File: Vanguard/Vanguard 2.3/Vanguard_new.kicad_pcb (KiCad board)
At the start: 4 copper layers, 42.1 x 52.7 mm, 85 parts, among them J1 USB_C_Receptacle_USB2.0_16P, J2 Conn_02x03_Pin, J3 Micro_SD_Card_Det1, J4 STARBOARD_SERVO, J5 PORTSIDE_SERVO, J6 Conn_01x02_Pin, J7 EJECTION_SERVO, Q1 BSS138, Q2 BSS138, Q3 BSS138, Q4 BSS138, U1 ATSAMD11D14A-M, U2 ATmega4809-A, U3 AT25DF641A-SH-T, U4 AP2112K-3.3, U5 BD1020HFV, U6 BNO086, U7 TXB0104D, U8 TPS61092, U9 MPM3610AGQV-P, Y1 32.768kHz

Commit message: done pcb
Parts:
- moved TP1 0.08 mm to (113.2, 92.5)
- moved TP2 0.05 mm to (114.7, 93.9)
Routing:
- net RX0: track 1.67 -> 41.4 mm, vias 0 -> 2
- net +3.3V: track 141.4 -> 167.0 mm, vias 14 -> 18
- net TX0: track 1.76 -> 23.2 mm, vias 0 -> 2
- net GND: track 104.7 -> 94.6 mm, vias 37 -> 41
- net Net-(D6-K): track 12.3 -> 15.6 mm
- net PORT_RED: track 27.0 -> 28.7 mm
- net CD: track 39.5 -> 40.7 mm
- net POWER_STAB: track 85.8 -> 86.9 mm
- net Net-(U9-EN): track 4.08 -> 4.92 mm
- net HOLD: track 16.1 -> 16.8 mm
- net PORT_SERVO: track 38.9 -> 39.5 mm
- removed copper zone on B.Cu, net (none)
- removed copper zone on F.Cu, net (none)

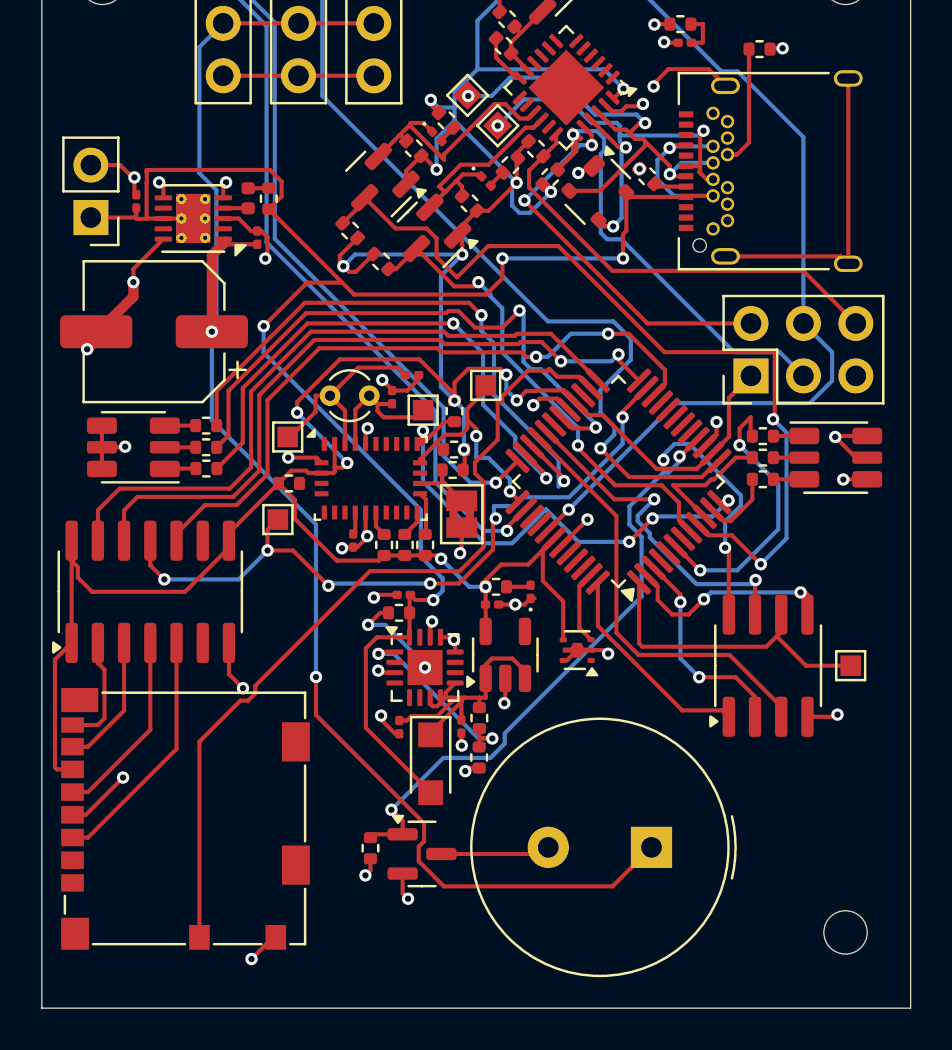
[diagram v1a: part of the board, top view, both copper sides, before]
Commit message: Centerd IMU
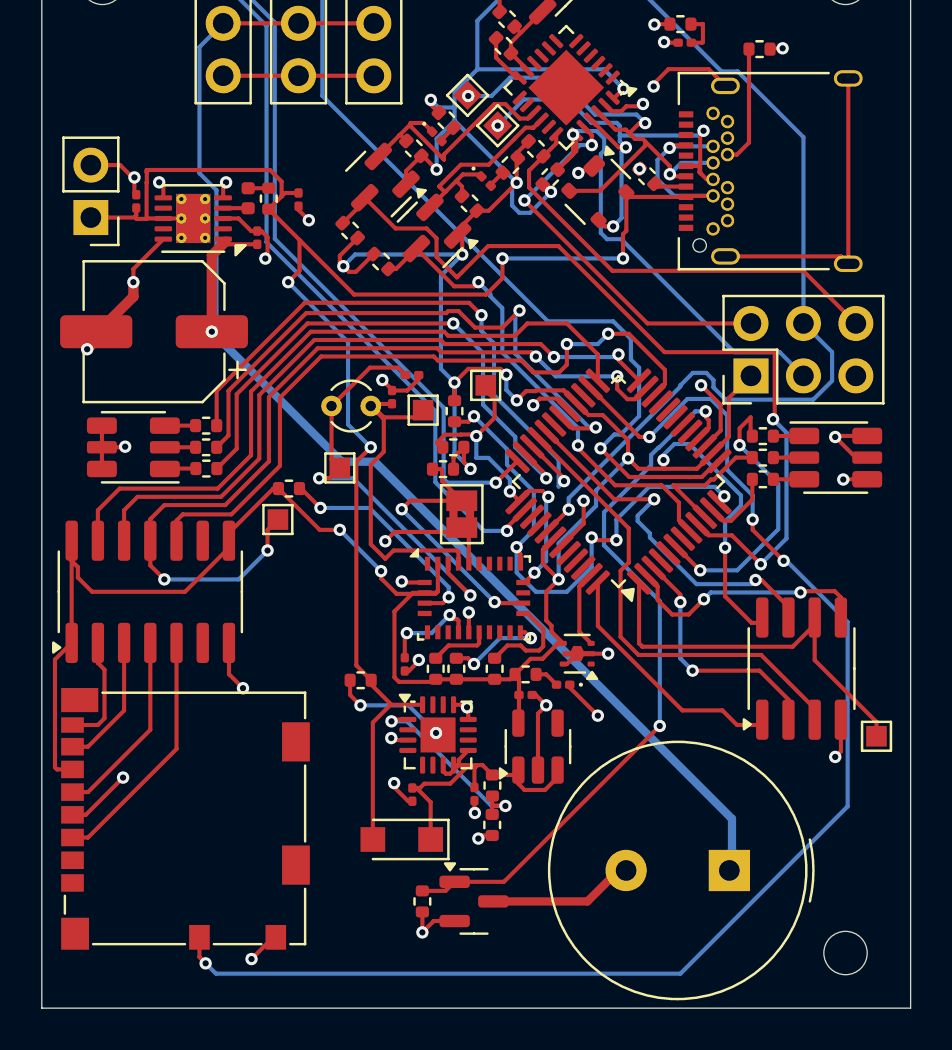
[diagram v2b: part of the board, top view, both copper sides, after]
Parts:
- moved C4 19.8 mm to (105.0, 97.5), turned to -90 degrees
- moved U6 7.66 mm to (113.5, 116.8)
- moved R20 6.88 mm to (114.5, 120.2)
- moved C7 6.50 mm to (110.1, 120.0)
- moved R18 6.50 mm to (111.6, 120.2)
- moved R19 6.50 mm to (112.6, 120.2)
- moved D5 4.77 mm to (117.8, 121.0), turned to 180 degrees
- moved U4 4.72 mm to (116.6, 124.0)
- moved C6 4.67 mm to (116.0, 121.5)
- moved R17 4.48 mm to (116.0, 120.5)
- moved BZ1 3.93 mm to (125.9, 130.0)
- moved D6 3.93 mm to (110.0, 128.5), turned to 180 degrees
- moved R14 3.76 mm to (108.0, 120.8)
- moved TP4 3.64 mm to (133.0, 123.5)
- moved R34 3.60 mm to (111.0, 131.5)
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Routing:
- net CD: track 40.7 -> 66.2 mm, vias 0 -> 4
- net Net-(U6-~{BOOT}): track 0.00 -> 11.0 mm, vias 0 -> 2
- net Net-(U6-XIN32): track 10.3 -> 20.5 mm, vias 0 -> 2
- net Net-(ADR1-B): track 3.06 -> 13.2 mm, vias 0 -> 2
- net Net-(U6-XOUT32/CLKSEL1): track 6.71 -> 16.4 mm
- net GND: track 94.6 -> 103.6 mm, vias 41 -> 38
- net D4: track 34.7 -> 41.4 mm, vias 6 -> 4
- net BUZZER: track 29.1 -> 35.1 mm
- net +5V: track 72.2 -> 66.6 mm, vias 2 -> 1
- net SCL: track 11.3 -> 16.5 mm, vias 2 -> 4
- net PA2/SCK: track 15.2 -> 19.3 mm
- net Net-(U6-CAP): track 1.07 -> 4.78 mm, vias 0 -> 2
- net Net-(U6-ENV_SCL): track 1.31 -> 4.87 mm, vias 0 -> 2
- net +3.3V: track 167.0 -> 169.9 mm
- net Net-(U6-ENV_SDA): track 2.11 -> 4.92 mm
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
